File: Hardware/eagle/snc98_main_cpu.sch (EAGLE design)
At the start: 88 parts, among them IC1 MCP170333MB, M1 IRLML2244, M12 IRLML2244, M2 IRLML2244, M3 IRLML2244, T1 BCR135, T2 BCR135, T3 BCR185, U1 74HC4051_MUX, U2 DS18B20, U3 ATMEGA1284P-PU, U4 TLV70033 / TC1185, Y2 12MHz

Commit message: Gerber file added
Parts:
- added C17, C19: 1µ, rcl:C-EUC1206K
- added C23: 220n, SparkFun:CAP0805
- BH9: TME_EU (none) -> BC-0401
- C10, C22, C6: TME_EU (none) -> CC0805KRX7R9153
- C13, C5: TME_EU (none) -> CC0805KRX7R9473
- C18: TME_EU (none) -> CC0805KPX7R7224
- C20, C21: value 4.7uF -> 1uF
- C7, C8: value 15pF -> 22pF; TME_EU (none) -> CL21C220JBANNNC
- M1: TME_EU (none) -> DMG2305UX-7
- R1, R28, R46: TME_EU (none) -> CRCW080547K0FKTABC
- R21, R22, R23, R27, R3, R34, R50, R7: TME_EU (none) -> RC0805FR-076K8
- R25: value 100 -> 47
- R31, R32: TME_EU (none) -> CRCW0805150RJNTABC
- R35, R48, R51: TME_EU (none) -> RC0805FR-073K3
- R4: TME_EU (none) -> WF08P-100R-5%
- R44, R47, R6: TME_EU (none) -> CRCW080522K0FKTABC
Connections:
- net DTR: now also C23.2
- net GND: now also C17.2, C19.2
- net R_: now also C23.1
- net VCC: now also C17.1
- net V_IN: now also C19.1
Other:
- moved on the sheet: C20

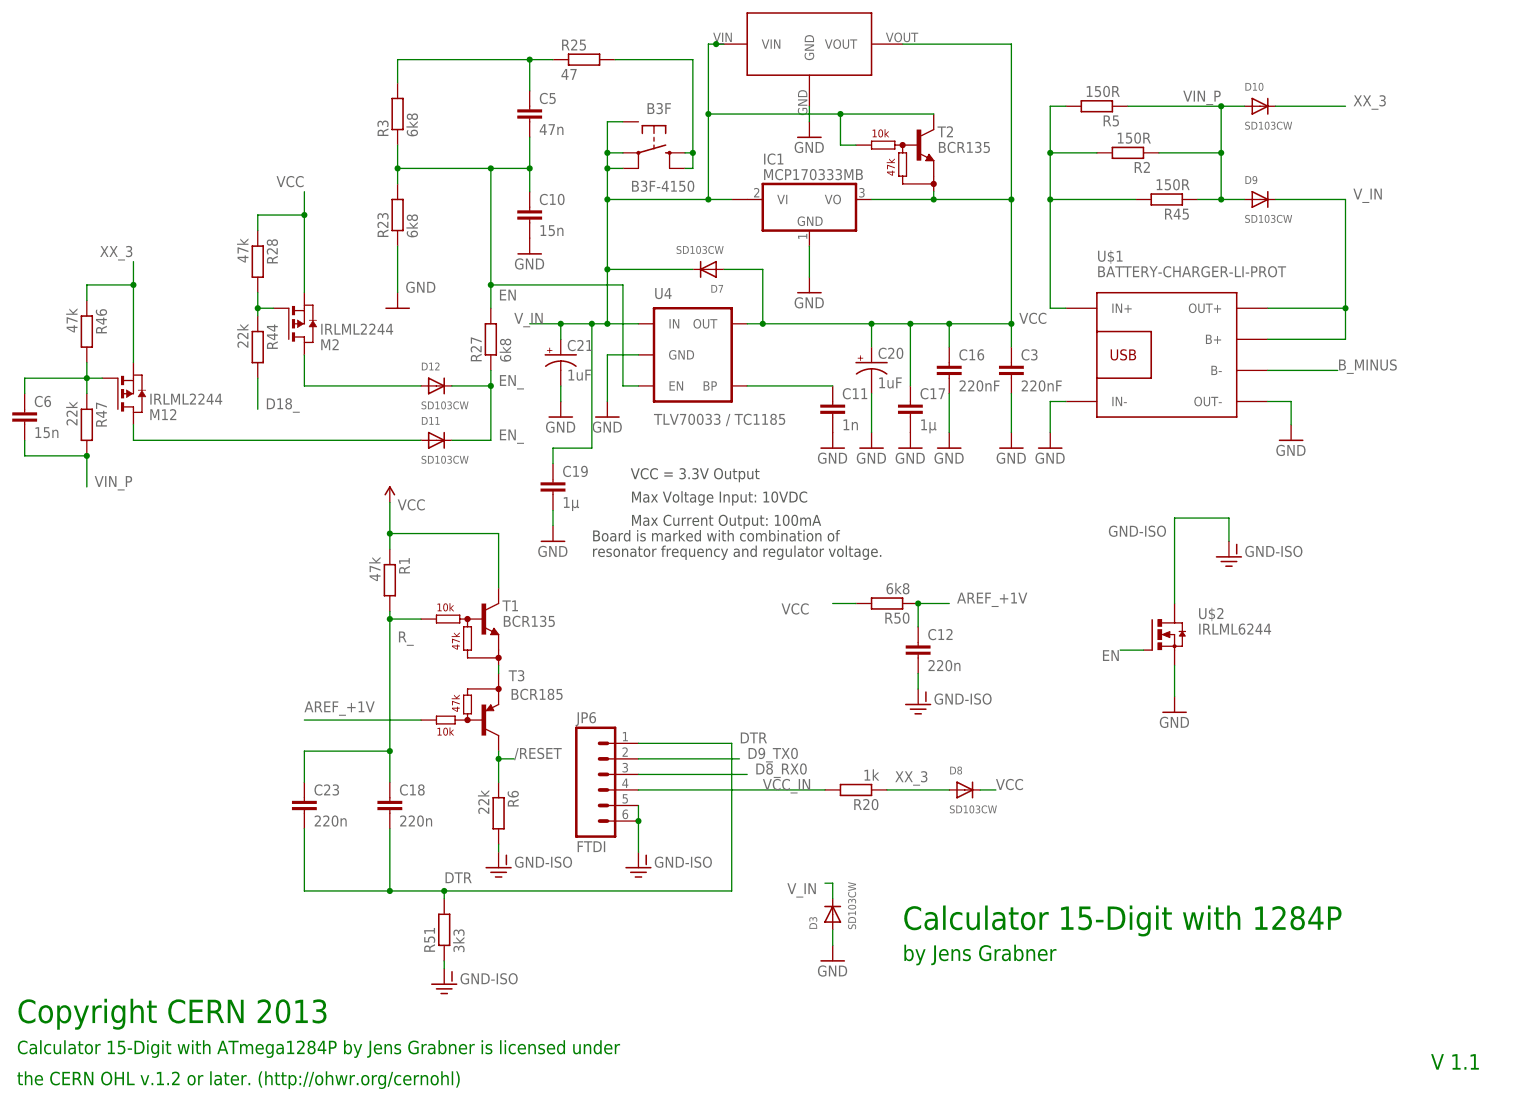
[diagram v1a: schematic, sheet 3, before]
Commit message: more accurate Factorial Function n!
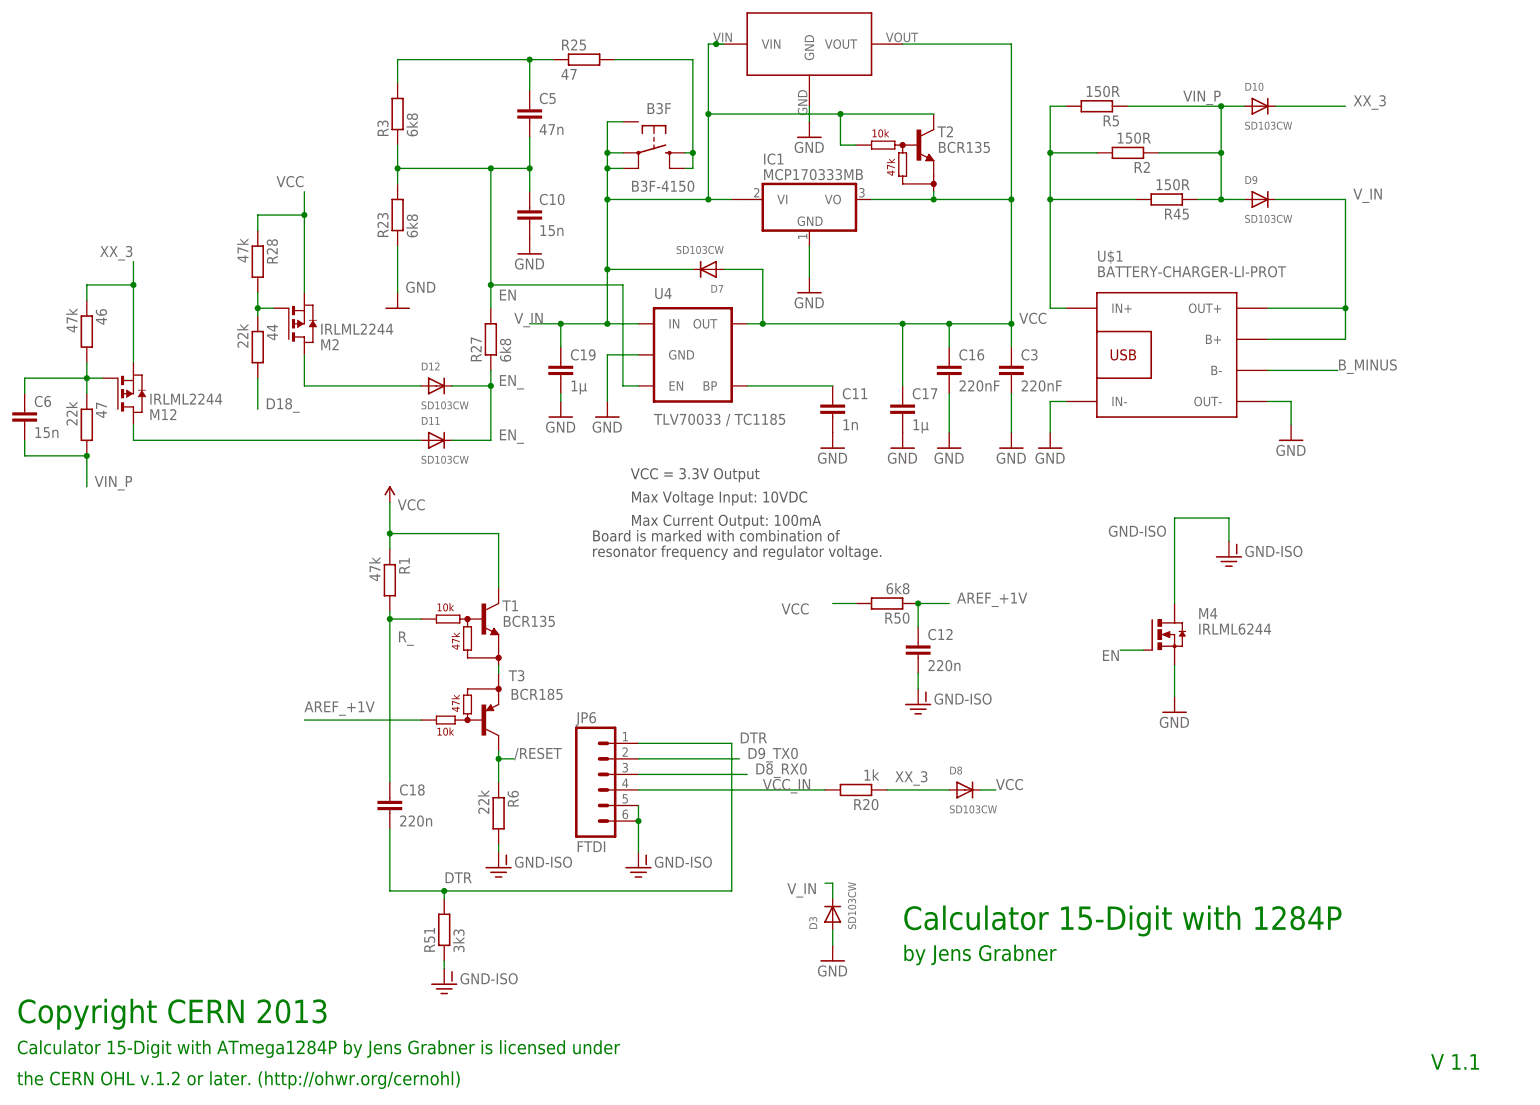
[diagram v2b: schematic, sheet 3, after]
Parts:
- removed C20, C21: 1uF, SparkFun:CAP_POL1206
- removed C23: 220n, SparkFun:CAP0805
- R4: value 100 -> 47
- renumbered R44 to 44, R46 to 46, R47 to 47, U$2 to M4
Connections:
- net DTR: no longer C23.2
- net GND: no longer C20.-, C21.-
- net R_: no longer C23.1
- net VCC: no longer C20.+
- net V_IN: no longer C21.+
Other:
- moved on the sheet: C17, C19

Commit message: cleanup_PCB
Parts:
- C3: value 220nF -> 1µ; device SparkFun:CAP0805 -> rcl:C-EUC1206K
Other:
- moved on the sheet: C3, JP6
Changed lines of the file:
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@@
 <attribute name="OC_FARNELL" value="unknown"/>
 </part>
-<part name="C3" library="SparkFun" deviceset="CAP" device="0805" value="220nF">
-<attribute name="MF" value=""/>
-<attribute name="MPN" value=""/>
-<attribute name="OC_FARNELL" value="unknown"/>
-</part>
-<part name="GND8" library="SparkFun" deviceset="GND" device=""/>
 <part name="C6" library="rcl" deviceset="C-EU" device="C1206K" value="15n">
 <attribute name="MF" value=""/>
@@
 </part>
 <part name="GND9" library="SparkFun" deviceset="GND" device=""/>
+<part name="C3" library="rcl" deviceset="C-EU" device="C1206K" value="1µ">
+<attribute name="MF" value=""/>
+<attribute name="MPN" value=""/>
+<attribute name="OC_FARNELL" value="unknown"/>
+</part>
 </parts>
 <sheets>
@@
 <attribute name="MPN" x="181.61" y="165.1" size="1.016" layer="96" align="bottom-center" display="off"/>
 </instance>
-<instance part="C3" gate="G$1" x="167.64" y="120.65">
-<attribute name="OC_FARNELL" x="167.64" y="120.65" size="1.016" layer="96" align="bottom-center" display="off"/>
-<attribute name="MF" x="167.64" y="120.65" size="1.016" layer="96" align="bottom-center" display="off"/>
-<attribute name="MPN" x="167.64" y="120.65" size="1.016" layer="96" align="bottom-center" display="off"/>
-</instance>
-<instance part="GND8" gate="1" x="167.64" y="109.22"/>
 <instance part="C6" gate="G$1" x="6.35" y="115.57">
 <attribute name="OC_FARNELL" x="6.35" y="115.57" size="1.016" layer="96" align="bottom-center" display="off"/>
@@
 </instance>
 <instance part="GND9" gate="1" x="93.98" y="114.3"/>
+<instance part="C3" gate="G$1" x="175.26" y="127">
+<attribute name="OC_FARNELL" x="175.26" y="127" size="1.016" layer="96" align="bottom-center" display="off"/>
+<attribute name="MF" x="175.26" y="127" size="1.016" layer="96" align="bottom-center" display="off"/>
+<attribute name="MPN" x="175.26" y="127" size="1.016" layer="96" align="bottom-center" display="off"/>
+</instance>
 </instances>
 <busses>
@@
 <segment>
 <pinref part="U$1" gate="G$1" pin="IN-"/>
-<wire x1="176.53" y1="116.84" x2="173.99" y2="116.84" width="0.1524" layer="91"/>
+<wire x1="176.53" y1="116.84" x2="175.26" y2="116.84" width="0.1524" layer="91"/>
+<wire x1="175.26" y1="116.84" x2="173.99" y2="116.84" width="0.1524" layer="91"/>
 <wire x1="173.99" y1="116.84" x2="173.99" y2="111.76" width="0.1524" layer="91"/>
 <pinref part="GND3" gate="1" pin="GND"/>
+<pinref part="C3" gate="G$1" pin="2"/>
+<wire x1="175.26" y1="121.92" x2="175.26" y2="116.84" width="0.1524" layer="91"/>
+<junction x="175.26" y="116.84"/>
 </segment>
 <segment>
@@
 <pinref part="M4" gate="G$1" pin="S"/>
 <wire x1="194.31" y1="73.66" x2="194.31" y2="68.58" width="0.1524" layer="91"/>
-</segment>
-<segment>
-<pinref part="C3" gate="G$1" pin="2"/>
-<pinref part="GND8" gate="1" pin="GND"/>
-<wire x1="167.64" y1="118.11" x2="167.64" y2="111.76" width="0.1524" layer="91"/>
 </segment>
 <segment>
@@
 <wire x1="167.64" y1="175.26" x2="167.64" y2="149.86" width="0.1524" layer="91"/>
 <junction x="167.64" y="149.86"/>
-<pinref part="C3" gate="G$1" pin="1"/>
-<wire x1="167.64" y1="125.73" x2="167.64" y2="129.54" width="0.1524" layer="91"/>
 <junction x="167.64" y="129.54"/>
 <pinref part="T2" gate="T$1" pin="E"/>
@@
 <wire x1="149.86" y1="119.38" x2="149.86" y2="129.54" width="0.1524" layer="91"/>
 <junction x="149.86" y="129.54"/>
-</segment>
-<segment>
+<pinref part="C3" gate="G$1" pin="1"/>
+<wire x1="175.26" y1="129.54" x2="167.64" y2="129.54" width="0.1524" layer="91"/>
+</segment>
+<segment>

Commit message: cbrt_int96
cbrt added
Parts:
- D10, D11, D12, D3, D4, D5, D7, D8, D9: device BaseApp:DIODESMA -> BaseApp:DIODESOD-123F
